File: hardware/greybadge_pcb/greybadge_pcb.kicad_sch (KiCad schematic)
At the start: 100 parts, among them J2 Conn_02x05_Row_Letter_First, J3 Conn_02x05_Row_Letter_First, J4 Conn_02x05_Row_Letter_First, J5 78171-0002, Q1 2N7002, SW1 SW_SPST, SW2 SW_Push, SW3 SW_Push, SW4 SW_Push, SW5 SW_Push, SW6 SW_Push, SW7 SW_Push, SW8 SW_Push, U1 GC9A01_IPS_display, U2 BQ24075, U3 TLV62568DBV, U4 TLV62568DBV, U5 TLV73325PDBV

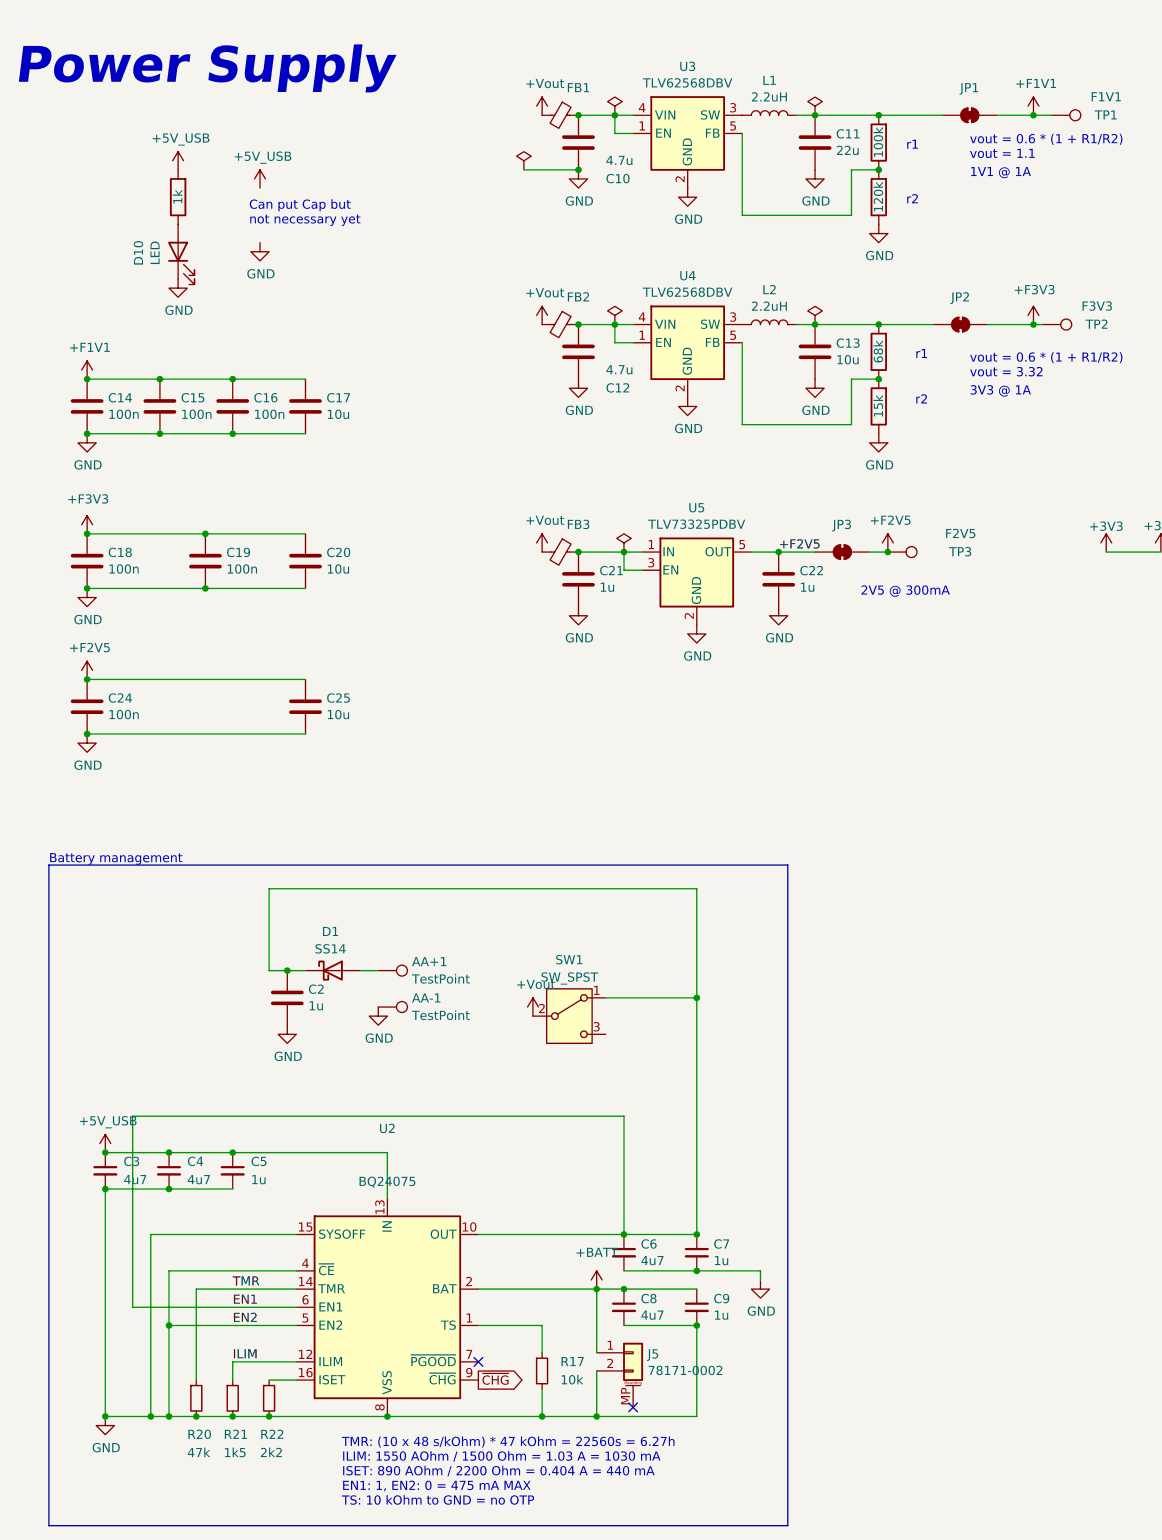
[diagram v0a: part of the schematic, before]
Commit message: Remove USB LED, add LED charging indicator
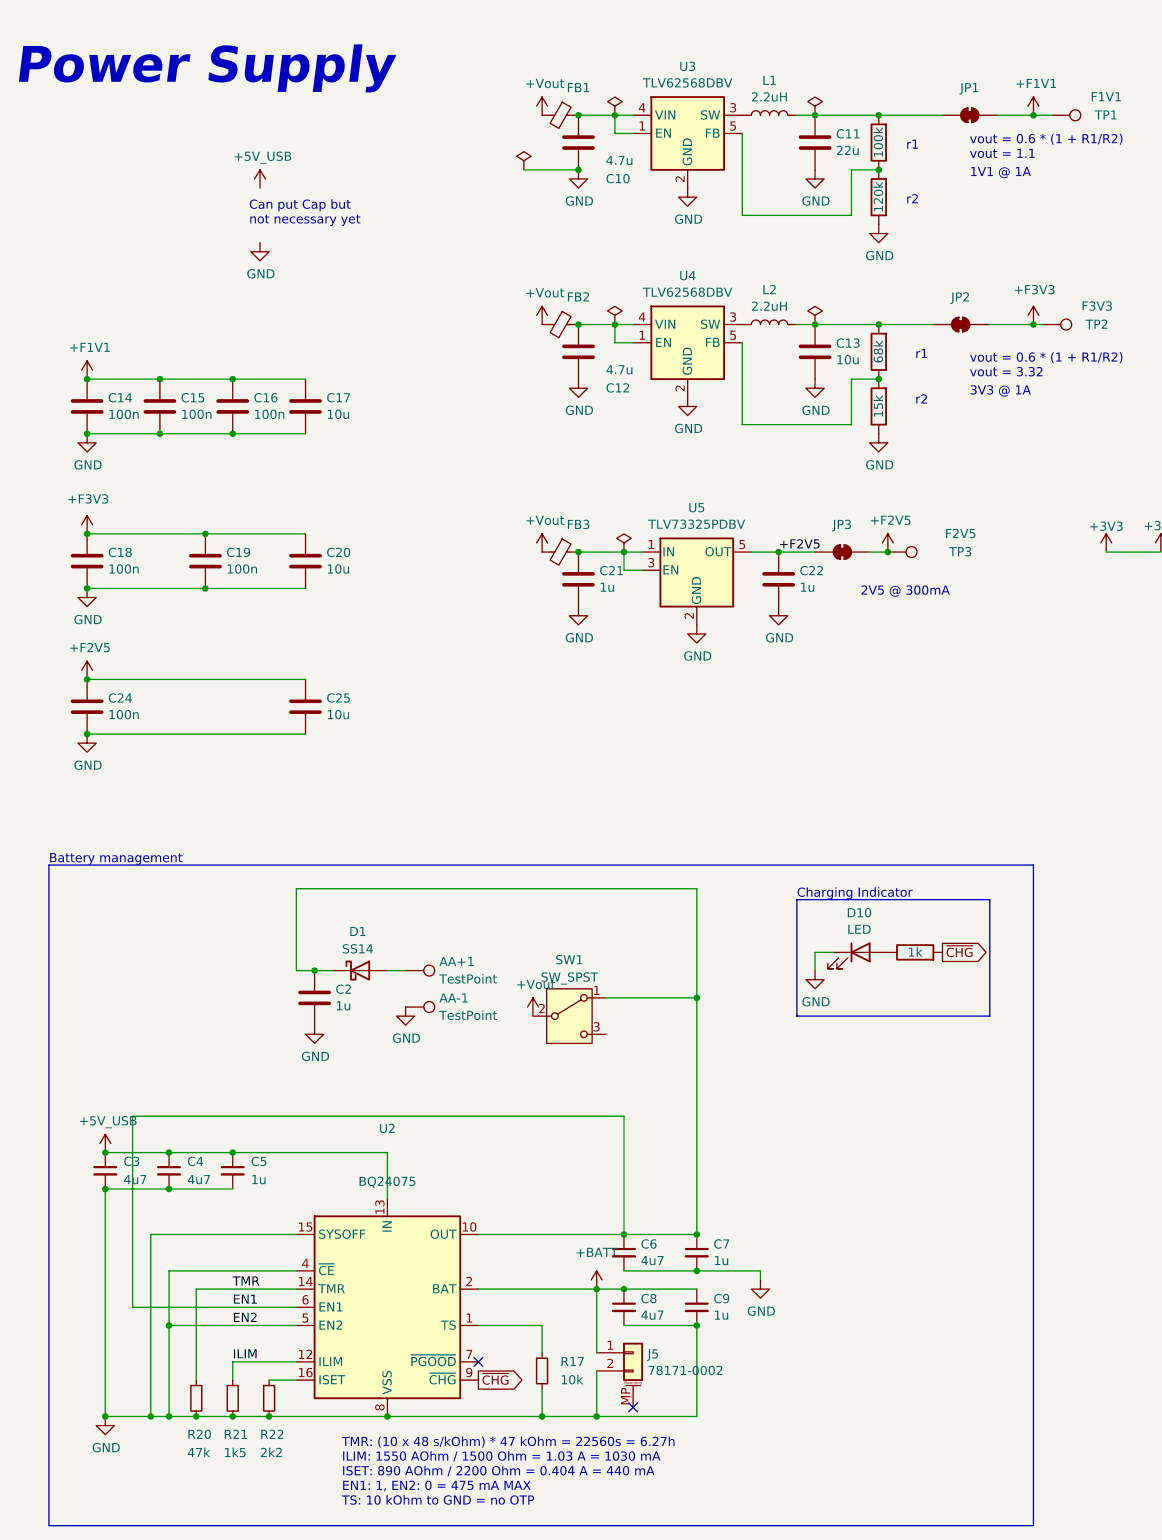
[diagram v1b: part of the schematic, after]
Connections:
- net +5V_USB: no longer R24.2
- net ~{CHG}: now also R24.2
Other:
- note added: "Charging Indicator"
- moved on the sheet: AA+1, AA-1, C2, D1, D10

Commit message: Fix prev commit
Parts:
- renumbered C10 to C1, C19 to C10, C20 to C11, C21 to C12, C22 to C13, C23 to C14, C24 to C15, C25 to C16, C2 to C17, C1 to C18, C3 to C19, C11 to C2, C4 to C20, C5 to C21, C6 to C22, C7 to C23, C8 to C24, C9 to C25, C12 to C3, C13 to C4, C14 to C5, C15 to C6, C16 to C7, C17 to C8, C18 to C9, D2 to D1, D1 to D10, D3 to D2, D4 to D3, D5 to D4, D6 to D5, D7 to D6, D8 to D7, D9 to D8, D10 to D9, J2 to J1, J3 to J2, J4 to J3, J5 to J4, JP4 to JP1, JP5 to JP2, JP6 to JP3, JP7 to JP4, JP8 to JP5, JP1 to JP6, JP2 to JP7, JP3 to JP8, R4 to R1, R13 to R10, R14 to R11, R15 to R12, R16 to R13, R18 to R14, R19 to R15, R23 to R16, R25 to R17, R26 to R18, R27 to R19, R5 to R2, R24 to R20, R1 to R21, R2 to R22, R17 to R23, R20 to R24, R21 to R25, R22 to R26, R6 to R3, R7 to R4, R8 to R5, R9 to R6, R10 to R7, R11 to R8, R12 to R9, SW2 to SW1, SW3 to SW2, SW4 to SW3, SW5 to SW4, SW6 to SW5, SW7 to SW6, SW8 to SW7, SW1 to SW8, U3 to U1, U4 to U2, U5 to U3, U1 to U4, U2 to U5

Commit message: feat: shift button resistors
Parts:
- removed C4: 10u, Capacitor_SMD:C_0402_1005Metric, symbol Device:C
- removed L2: 2.2uH, Inductor_SMD:L_Taiyo-Yuden_NR-40xx, symbol Device:L
- removed R18: 68k, Resistor_SMD:R_0805_2012Metric, symbol Device:R
- removed R19: 15k, Resistor_SMD:R_0805_2012Metric, symbol Device:R
- removed U2: TLV62568DBV, Package_TO_SOT_SMD:SOT-23-5, symbol Regulator_Switching:TLV62568DBV
- added U10: AMS1117-3.3, Maibadge_Howard:SOT-89-3_L4.5-W2.5-P1.50-LS4.2-BR, symbol AM1117:AMS1117-3.3
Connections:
- net +F3V3 is gone; now on net +3V3: C10.1, C11.1, C9.1, J1.1 (Pin_1), J1.2 (Pin_2), J2.1 (Pin_1), J2.2 (Pin_2), JP7.2 (B), R1.1, R13.1, R22.2, R6.1, R8.1, R9.1, TP2.1
- net GND: now also U10.1 (GND/ADJ)
- net at C3.1, FB2.1: now also U10.3 (VIN)
- net at JP7.1 (A): now also U10.2 (VOUT)
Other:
- moved on the sheet: JP7, TP2

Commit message: feat: stuff
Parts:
- removed C14: 10u, Capacitor_SMD:C_0402_1005Metric, symbol Device:C
- removed C2: 22u, Capacitor_SMD:C_0402_1005Metric, symbol Device:C
- removed L1: 2.2uH, Inductor_SMD:L_Taiyo-Yuden_NR-40xx, symbol Device:L
- removed R16: 100k, Resistor_SMD:R_0805_2012Metric, symbol Device:R
- removed R17: 120k, Resistor_SMD:R_0805_2012Metric, symbol Device:R
- removed U1: TLV62568DBV, Package_TO_SOT_SMD:SOT-23-5, symbol Regulator_Switching:TLV62568DBV
- added U2: TLV73311PDBV, Package_TO_SOT_SMD:SOT-23-5, symbol Regulator_Linear:TLV73311PDBV
- U10: footprint Maibadge_Howard:SOT-89-3_L4.5-W2.5-P1.50-LS4.2-BR -> custom:SOT-89-3_L4.5-W2.5-P1.50-LS4.2-BR
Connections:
- net GND: now also U2.2 (GND)
- net at C1.1, FB1.1: now also U2.1 (IN), U2.3 (EN)
- net at JP6.1 (A): now also U2.5 (OUT)
- net GPIO1 renamed C12
- net GPIO7 renamed D12
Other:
- note added: "1V1 @ 300mA"
- note removed: "1V1 @ 1A"
- note removed: "r1"
- note removed: "r2"
- note removed: "vout = 0.6 * (1 + R1/R2) vout = 1.1"

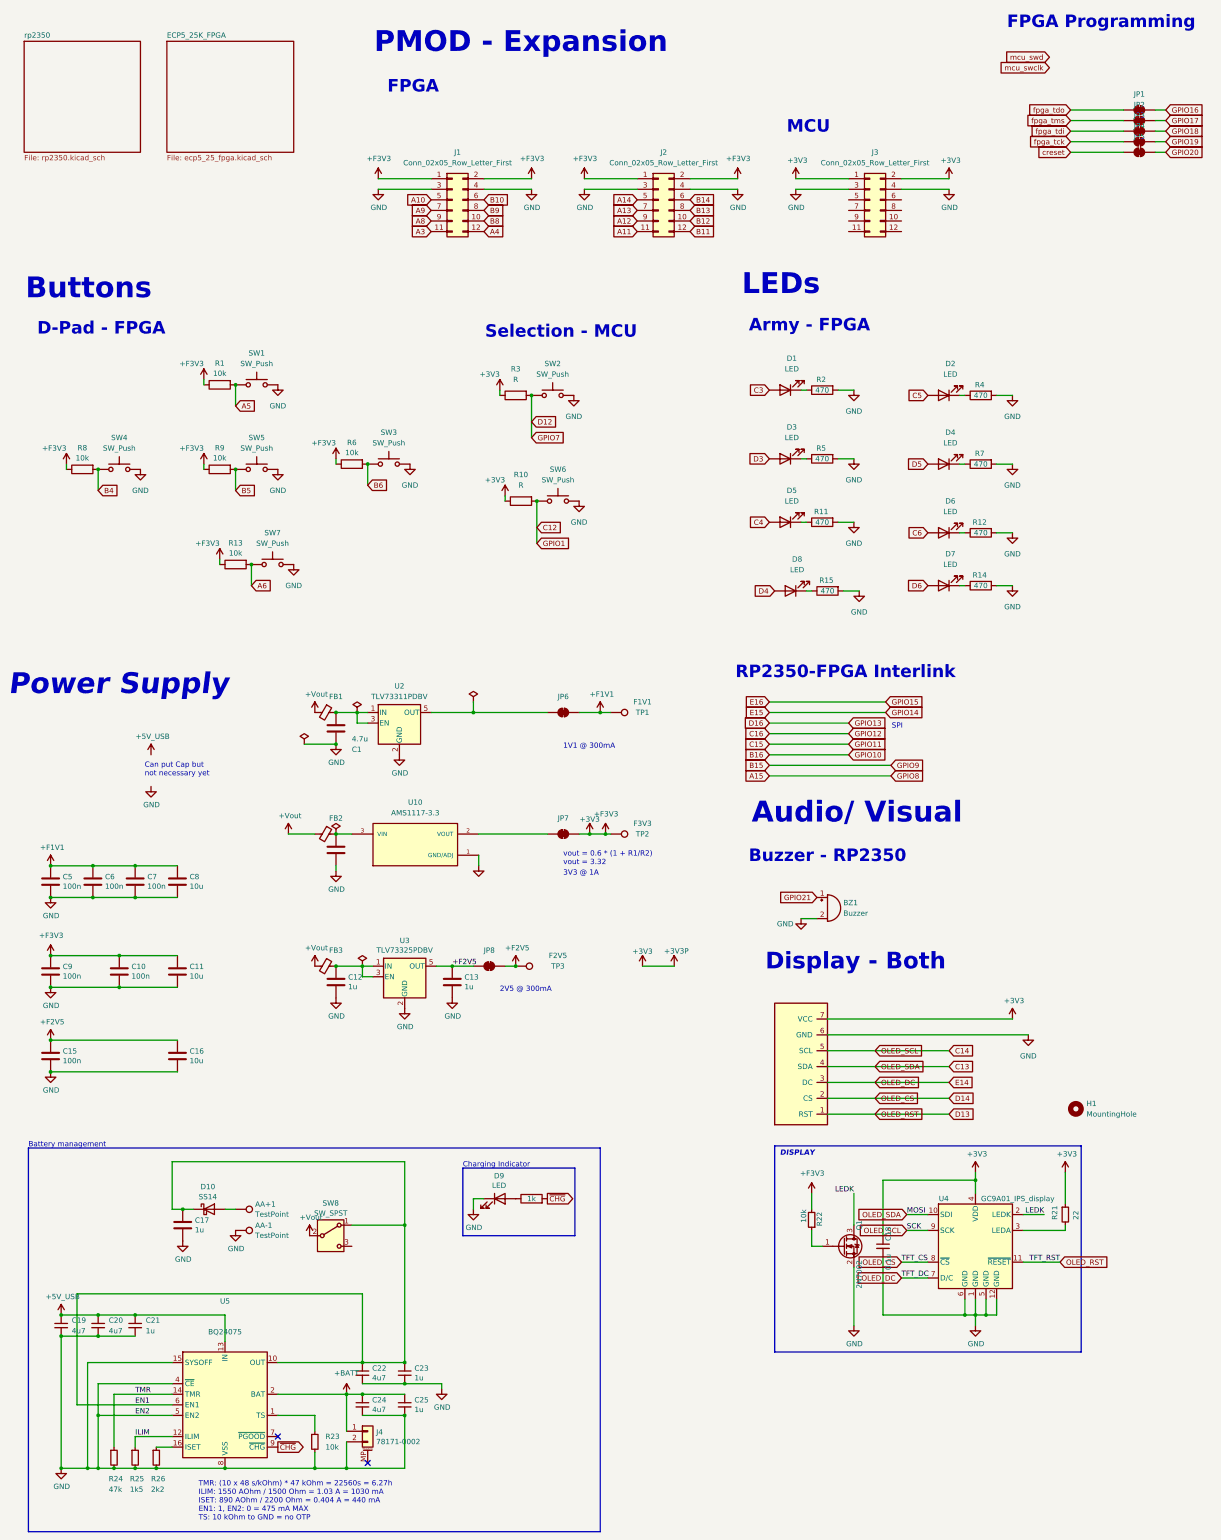
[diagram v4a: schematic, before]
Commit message: Route ADC and power, cleanup routing/silkscreen
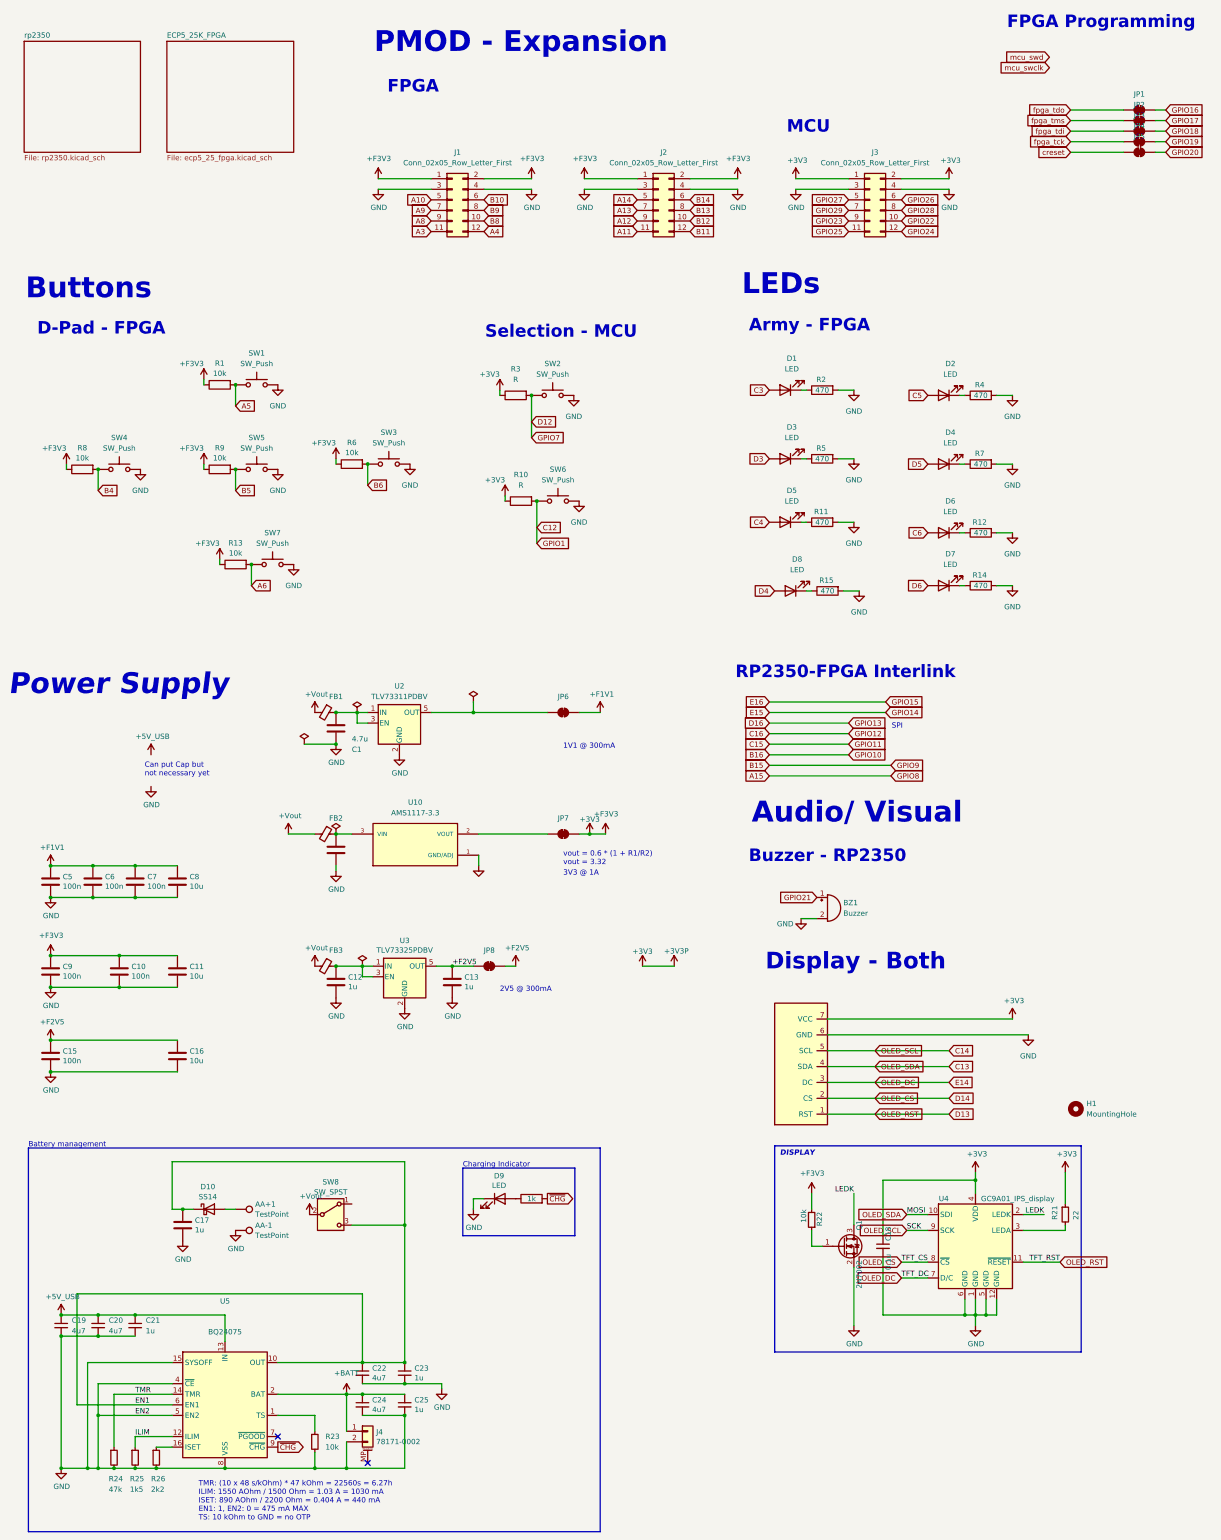
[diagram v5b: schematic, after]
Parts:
- removed TP1: F1V1, TestPoint:TestPoint_THTPad_D1.0mm_Drill0.5mm, symbol Connector:TestPoint
- removed TP2: F3V3, TestPoint:TestPoint_THTPad_D1.0mm_Drill0.5mm, symbol Connector:TestPoint
- removed TP3: F2V5, TestPoint:TestPoint_THTPad_D1.0mm_Drill0.5mm, symbol Connector:TestPoint
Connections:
- net EN1: now also SW8.3 (C); no longer SW8.1 (A)
- net GPIO22: now reaches J3.10 (Pin_10)
- net GPIO25: now reaches J3.11 (Pin_11)
- net GPIO24: now reaches J3.12 (Pin_12)
- net GPIO27: now reaches J3.5 (Pin_5)
- net GPIO26: now reaches J3.6 (Pin_6)
- net GPIO29: now reaches J3.7 (Pin_7)
- net GPIO28: now reaches J3.8 (Pin_8)
- net GPIO23: now reaches J3.9 (Pin_9)
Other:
- moved on the sheet: SW8
